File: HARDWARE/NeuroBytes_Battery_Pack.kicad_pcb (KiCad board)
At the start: 2 copper layers, 61 x 56.7 mm, 20 parts, among them P1 JST_GH_5-pos, P2 JST_GH_5-pos, SW1 Switch_SPDT, U1 LDL212_LDO

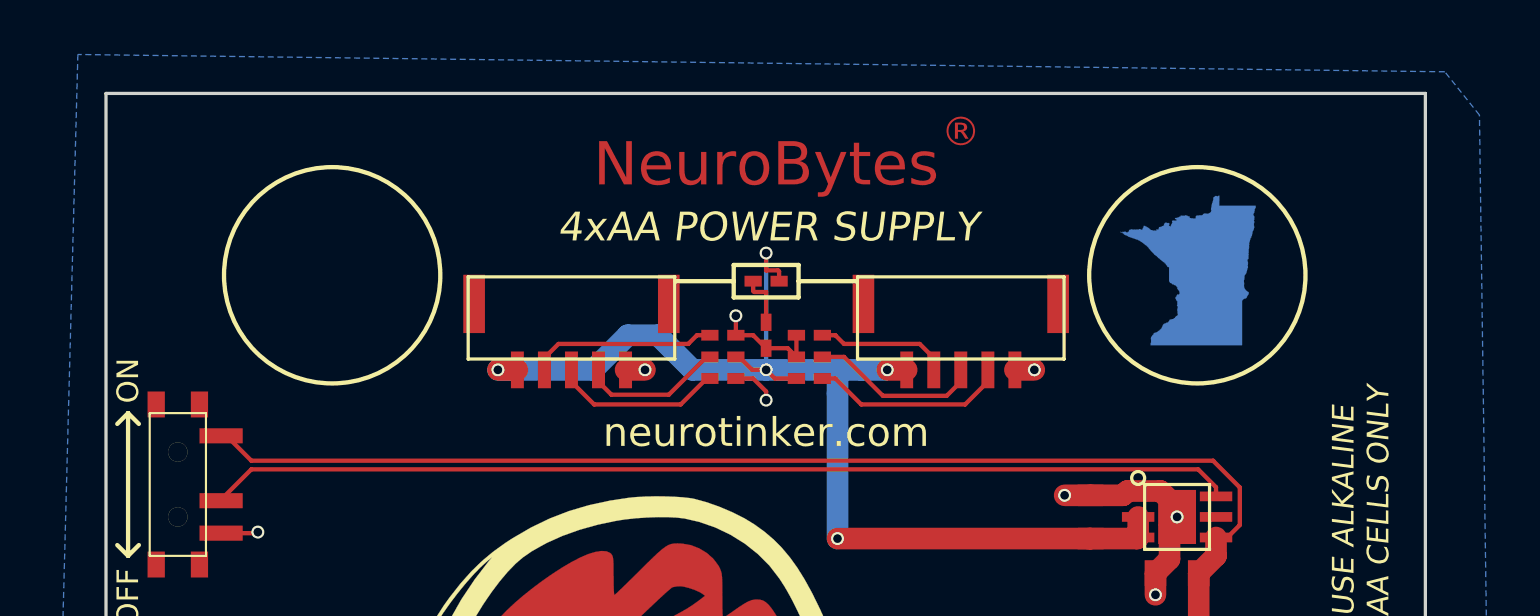
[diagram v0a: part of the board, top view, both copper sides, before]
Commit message: added copper fill and via stitching around JST GH structural pads
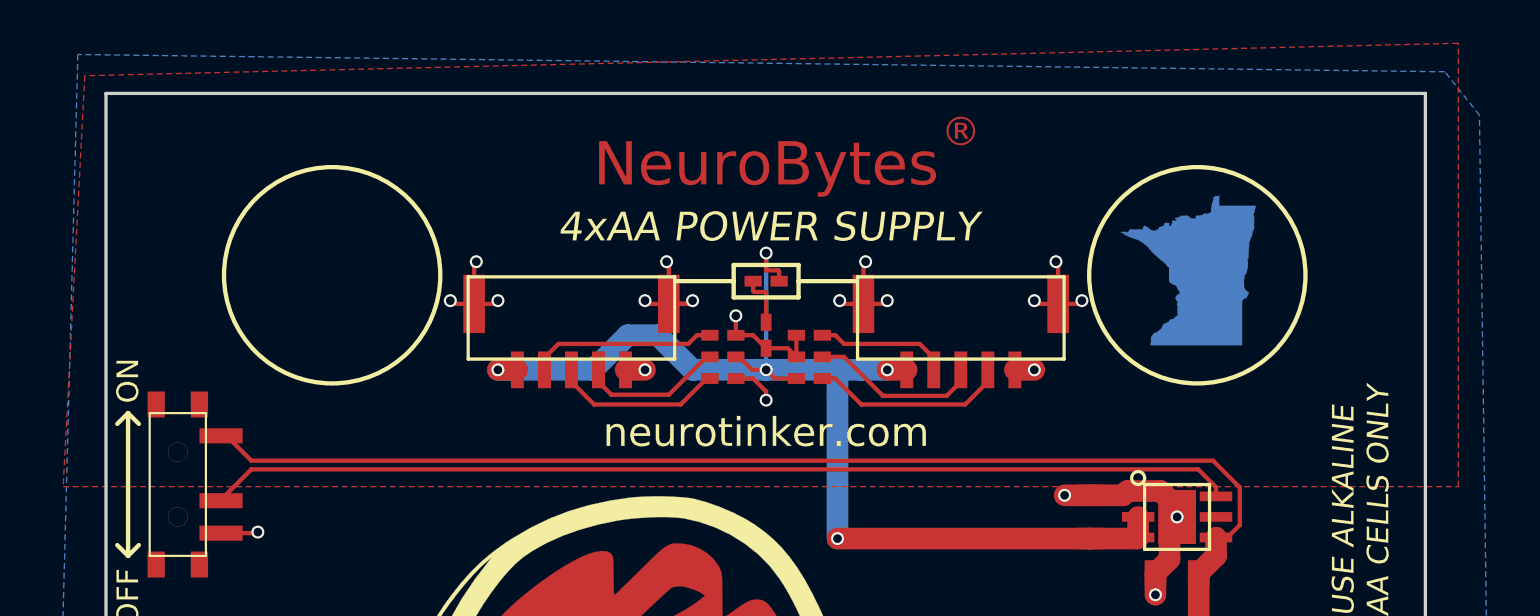
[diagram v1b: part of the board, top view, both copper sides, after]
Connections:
- P1 pad : (no net) -> GND
- P2 pad : (no net) -> GND
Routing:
- net GND: track 20.7 -> 38.8 mm, vias 8 -> 20
- added copper zone on F.Cu, net GND
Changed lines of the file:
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@@
     (thickness 1.6)
     (drawings 88)
-    (tracks 123)
+    (tracks 160)
     (zones 0)
     (modules 20)
@@
     (mod_text_size 1 1)
     (mod_text_width 0.15)
-    (pad_size 1.524 1.524)
-    (pad_drill 0.762)
+    (pad_size 1 2.7)
+    (pad_drill 0)
     (pad_to_mask_clearance 0)
     (aux_axis_origin 0 0)
@@
       (drillshape 0)
       (scaleselection 1)
-      (outputdirectory ""))
+      (outputdirectory ../../../NeuroTinker_RFQ_07202018/PCBAs/ZF-11268_NeuroBytes_Battery_Pack/))
   )
   (net 0 "")
@@
     (pad 1 smd rect (at -1.6 2.5 180) (size 0.6 1.7) (layers F.Cu F.Paste F.Mask)
       (net 2 GND))
-    (pad "" smd rect (at 1.45 -4.5 180) (size 1 2.7) (layers F.Cu F.Paste F.Mask))
-    (pad "" smd rect (at 1.45 4.5 180) (size 1 2.7) (layers F.Cu F.Paste F.Mask))
+    (pad "" smd rect (at 1.45 -4.5 180) (size 1 2.7) (layers F.Cu F.Paste F.Mask)
+      (net 2 GND))
+    (pad "" smd rect (at 1.45 4.5 180) (size 1 2.7) (layers F.Cu F.Paste F.Mask)
+      (net 2 GND))
     (pad 5 smd rect (at -1.6 -2.5 90) (size 1.7 0.6) (layers F.Cu F.Paste F.Mask)
       (net 7 "Net-(C2-Pad1)"))
@@
     (pad 1 smd rect (at -1.6 2.5 180) (size 0.6 1.7) (layers F.Cu F.Paste F.Mask)
       (net 2 GND))
-    (pad "" smd rect (at 1.45 -4.5 180) (size 1 2.7) (layers F.Cu F.Paste F.Mask))
-    (pad "" smd rect (at 1.45 4.5 180) (size 1 2.7) (layers F.Cu F.Paste F.Mask))
+    (pad "" smd rect (at 1.45 -4.5 180) (size 1 2.7) (layers F.Cu F.Paste F.Mask)
+      (net 2 GND))
+    (pad "" smd rect (at 1.45 4.5 180) (size 1 2.7) (layers F.Cu F.Paste F.Mask)
+      (net 2 GND))
     (pad 5 smd rect (at -1.6 -2.5 90) (size 1.7 0.6) (layers F.Cu F.Paste F.Mask)
       (net 7 "Net-(C2-Pad1)"))
@@
   (via (at 197 76.25) (size 0.6) (drill 0.4) (layers F.Cu B.Cu) (net 1))
   (segment (start 197.885867 90.227043) (end 197.885867 77.135867) (width 1) (layer B.Cu) (net 1))
+  (segment (start 161.5 45.55) (end 161.5 43.7) (width 0.2) (layer F.Cu) (net 2))
+  (segment (start 161.5 43.7) (end 161.6 43.6) (width 0.2) (layer F.Cu) (net 2))
+  (via (at 161.6 43.6) (size 0.6) (drill 0.4) (layers F.Cu B.Cu) (net 2))
+  (segment (start 170.5 45.55) (end 170.5 43.7) (width 0.2) (layer F.Cu) (net 2))
+  (segment (start 170.5 43.7) (end 170.4 43.6) (width 0.2) (layer F.Cu) (net 2))
+  (via (at 170.4 43.6) (size 0.6) (drill 0.4) (layers F.Cu B.Cu) (net 2))
+  (segment (start 179.5 45.55) (end 179.5 43.7) (width 0.2) (layer F.Cu) (net 2))
+  (segment (start 179.5 43.7) (end 179.6 43.6) (width 0.2) (layer F.Cu) (net 2))
+  (via (at 179.6 43.6) (size 0.6) (drill 0.4) (layers F.Cu B.Cu) (net 2))
+  (segment (start 188.5 45.55) (end 188.5 43.7) (width 0.2) (layer F.Cu) (net 2))
+  (segment (start 188.5 43.7) (end 188.4 43.6) (width 0.2) (layer F.Cu) (net 2))
+  (via (at 188.4 43.6) (size 0.6) (drill 0.4) (layers F.Cu B.Cu) (net 2))
+  (segment (start 188.5 45.55) (end 189.45 45.55) (width 0.2) (layer F.Cu) (net 2))
+  (segment (start 189.45 45.55) (end 189.6 45.4) (width 0.2) (layer F.Cu) (net 2))
+  (via (at 189.6 45.4) (size 0.6) (drill 0.4) (layers F.Cu B.Cu) (net 2))
+  (segment (start 188.5 45.55) (end 187.55 45.55) (width 0.2) (layer F.Cu) (net 2))
+  (segment (start 187.55 45.55) (end 187.4 45.4) (width 0.2) (layer F.Cu) (net 2))
+  (via (at 187.4 45.4) (size 0.6) (drill 0.4) (layers F.Cu B.Cu) (net 2))
+  (segment (start 179.5 45.55) (end 180.45 45.55) (width 0.2) (layer F.Cu) (net 2))
+  (segment (start 180.45 45.55) (end 180.6 45.4) (width 0.2) (layer F.Cu) (net 2))
+  (via (at 180.6 45.4) (size 0.6) (drill 0.4) (layers F.Cu B.Cu) (net 2))
+  (segment (start 179.5 45.55) (end 178.55 45.55) (width 0.2) (layer F.Cu) (net 2))
+  (segment (start 178.55 45.55) (end 178.4 45.4) (width 0.2) (layer F.Cu) (net 2))
+  (via (at 178.4 45.4) (size 0.6) (drill 0.4) (layers F.Cu B.Cu) (net 2))
+  (segment (start 161.5 45.55) (end 160.55 45.55) (width 0.2) (layer F.Cu) (net 2))
+  (segment (start 160.55 45.55) (end 160.4 45.4) (width 0.2) (layer F.Cu) (net 2))
+  (via (at 160.4 45.4) (size 0.6) (drill 0.4) (layers F.Cu B.Cu) (net 2))
+  (segment (start 161.5 45.55) (end 162.45 45.55) (width 0.2) (layer F.Cu) (net 2))
+  (segment (start 162.45 45.55) (end 162.6 45.4) (width 0.2) (layer F.Cu) (net 2))
+  (via (at 162.6 45.4) (size 0.6) (drill 0.4) (layers F.Cu B.Cu) (net 2))
+  (segment (start 170.5 45.55) (end 169.55 45.55) (width 0.2) (layer F.Cu) (net 2))
+  (segment (start 169.55 45.55) (end 169.4 45.4) (width 0.2) (layer F.Cu) (net 2))
+  (via (at 169.4 45.4) (size 0.6) (drill 0.4) (layers F.Cu B.Cu) (net 2))
+  (segment (start 170.5 45.55) (end 171.45 45.55) (width 0.2) (layer F.Cu) (net 2))
+  (segment (start 171.45 45.55) (end 171.6 45.4) (width 0.2) (layer F.Cu) (net 2))
+  (via (at 171.6 45.4) (size 0.6) (drill 0.4) (layers F.Cu B.Cu) (net 2))
+  (segment (start 170.5 45.55) (end 171.35 45.55) (width 0.2) (layer F.Cu) (net 2))
   (segment (start 175 49.6) (end 175 50) (width 0.2) (layer F.Cu) (net 2))
   (via (at 175 50) (size 0.6) (drill 0.4) (layers F.Cu B.Cu) (net 2))
@@
       )
     )
+  )
+  (zone (net 2) (net_name GND) (layer F.Cu) (hatch edge 0.508)
+    (connect_pads (clearance 0.2))
+    (min_thickness 0.2)
+    (fill yes (arc_segments 32) (thermal_gap 0.2) (thermal_bridge_width 1))
+    (polygon
+      (pts
+        (xy 143.5 35) (xy 142.5 54) (xy 207 54) (xy 207 33.5)
+      )
+    )
+  )
+  (zone (net 0) (net_name "") (layer F.Cu) (hatch edge 0.508)
+    (connect_pads (clearance 0.2))
+    (min_thickness 0.254)
+    (keepout (tracks allowed) (vias allowed) (copperpour not_allowed))
+    (fill yes (arc_segments 16) (thermal_gap 0.508) (thermal_bridge_width 0.508))
+    (polygon
+      (pts
+        (xy 165.5 35) (xy 165.5 41) (xy 186 41) (xy 186 35)
+      )
+    )

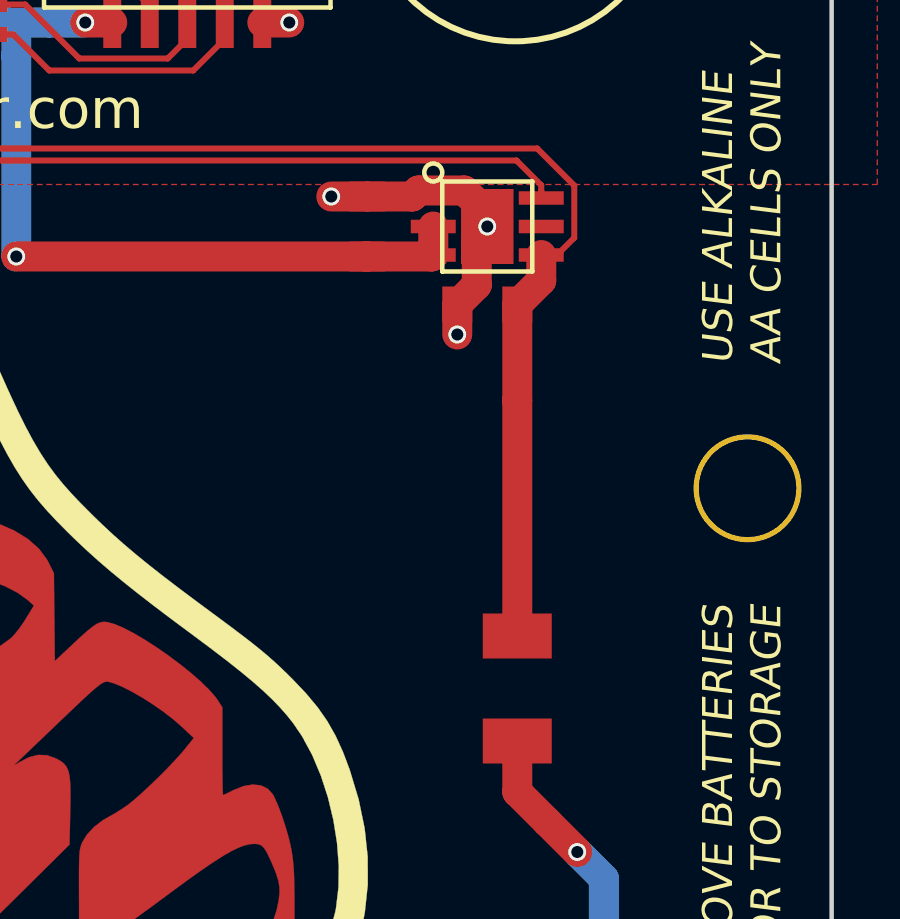
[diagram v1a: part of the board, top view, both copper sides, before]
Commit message: updated footprints to include outlines. re-generated Gerbers. added placement pdf.
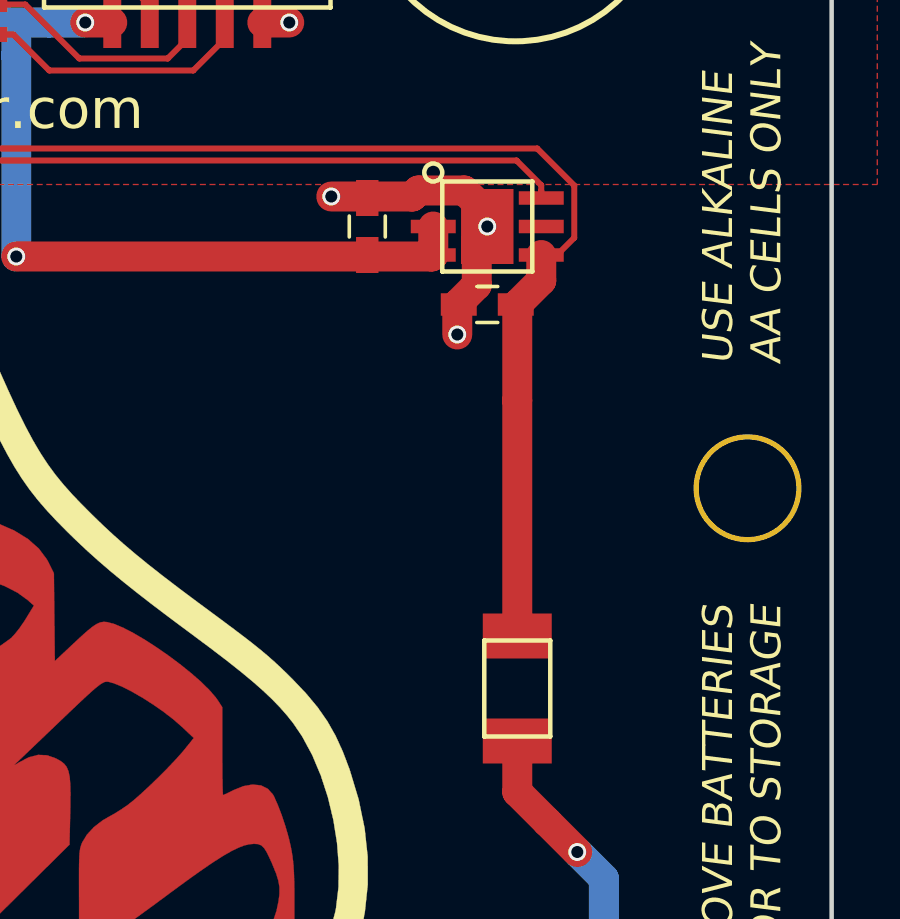
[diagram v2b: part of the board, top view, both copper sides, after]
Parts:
- C1, C2: footprint KiCad_Footprints:ZF_SMD_NonPol_0603 -> Capacitors_SMD:C_0603_HandSoldering
